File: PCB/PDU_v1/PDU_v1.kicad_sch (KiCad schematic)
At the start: 64 parts, among them J1 Conn_01x02_Pin, J10 Screw_Terminal_01x01, J11 Screw_Terminal_01x01, J12 Screw_Terminal_01x01, J13 Screw_Terminal_01x01, J14 Conn_01x04_Pin, J2 Screw_Terminal_01x01, J3 Screw_Terminal_01x01, J4 Screw_Terminal_01x01, J5 Screw_Terminal_01x01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

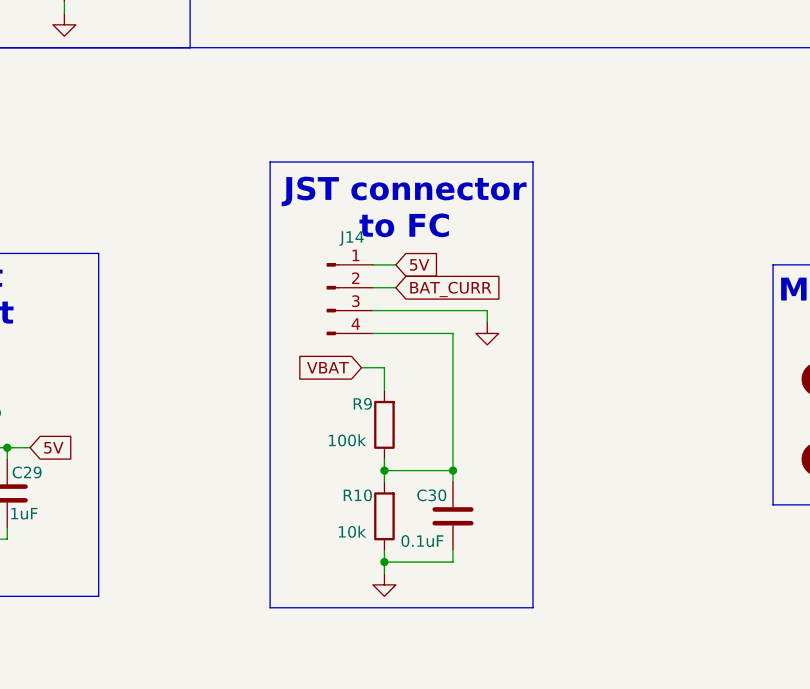
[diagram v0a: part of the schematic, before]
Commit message: Update PCB nets, footprint positions and routes
Rename and reassign nets for clarity (e.g. Net-(J14-Pin_4) -> BAT_VOL, adjust BAT_CURR and /BAT_IN/GND assignments), adjust component placement (C30 moved and value normalized from "0.1uF" to "100n"), and update board routing (track segment coordinates and UUIDs, zone polygon points). Add a PCB backup archive (PDU_v1-2026-02-05_204958.zip). These changes align footprints, nets and routing; schematic was also updated to keep the design consistent.
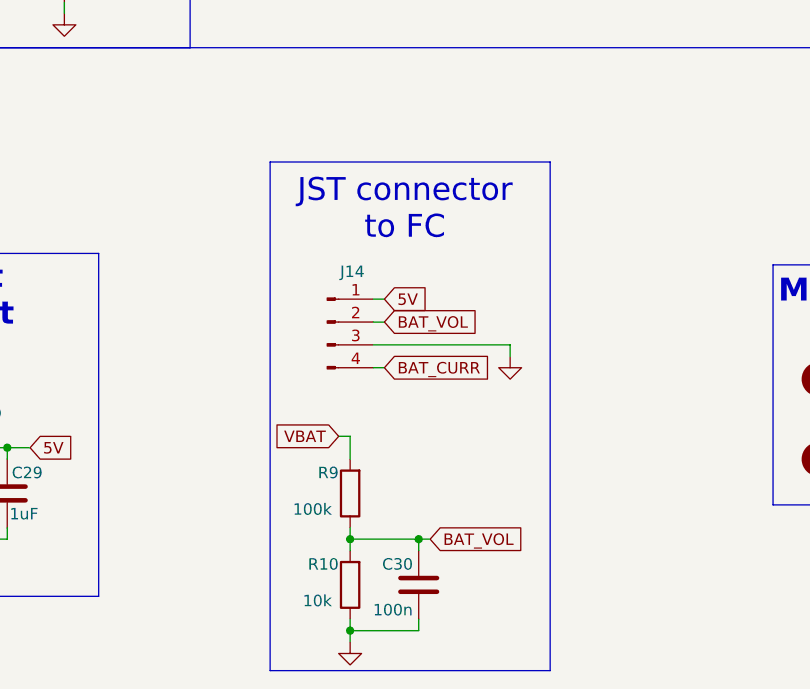
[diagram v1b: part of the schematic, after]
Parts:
- C30: value 0.1uF -> 100n
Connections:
- net BAT_CURR: now also J14.4 (Pin_4); no longer J14.2 (Pin_2)
- net BAT_VOL: now reaches C30.2, R10.2, R9.1
- net BAT_VOL: now also J14.2 (Pin_2); no longer J14.4 (Pin_4)
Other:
- moved on the sheet: C30, J14, R10, R9
